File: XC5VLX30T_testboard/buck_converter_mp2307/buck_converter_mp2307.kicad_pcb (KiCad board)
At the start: 2 copper layers, 18.5 x 11.8 mm, 12 parts, among them J1 Conn_02x01, J4 Conn_01x06_Pin, U1 MP2307DN-LF-Z

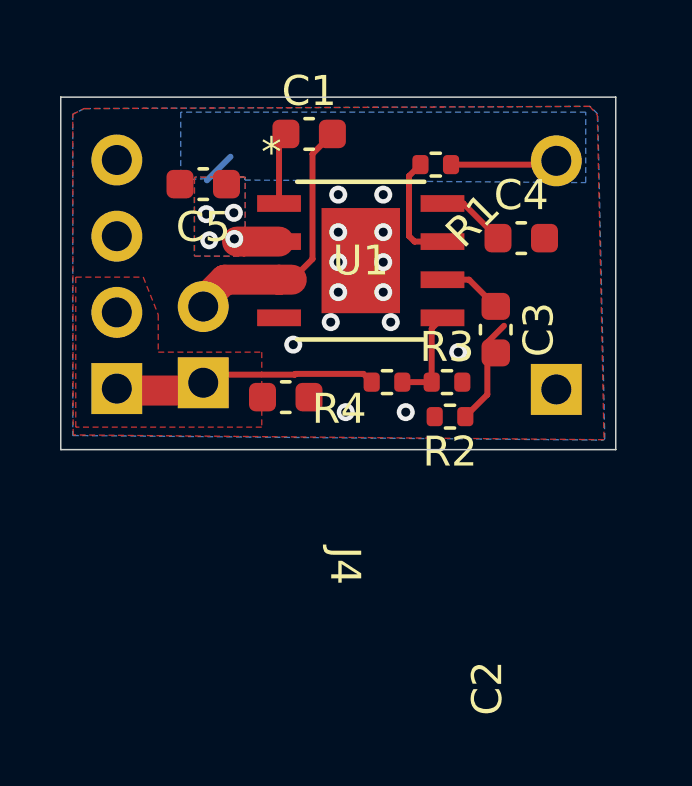
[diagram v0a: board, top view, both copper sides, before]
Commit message: reordered headers
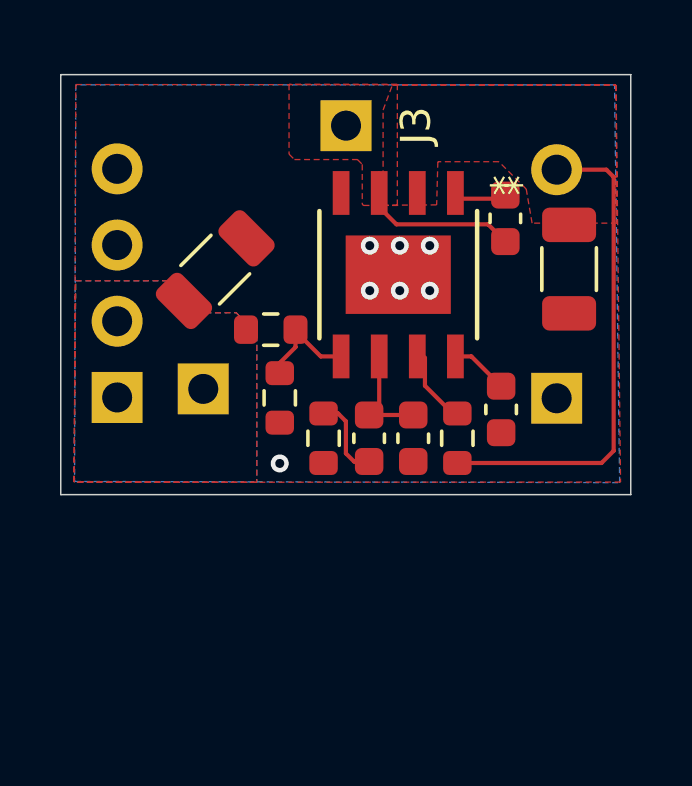
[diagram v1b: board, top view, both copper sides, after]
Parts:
- removed C5: 22uF, Capacitor_SMD:C_0603_1608Metric
- removed J1: Conn_02x01, Connector_PinHeader_2.54mm:PinHeader_2x01_P2.54mm_Vertical
- added C6: 0.1uF, Capacitor_SMD:C_0603_1608Metric, F.Cu at (117.5, 91.4)
- added C8: 22uF, Capacitor_SMD:C_1206_3216Metric, F.Cu at (122.7, 85.7)
- added J2: Inductor L, Connector_PinHeader_2.54mm:PinHeader_1x01_P2.54mm_Vertical, F.Cu at (110.5, 89.7)
- added J3: Inductor_R, Connector_PinHeader_2.54mm:PinHeader_1x01_P2.54mm_Vertical, F.Cu at (115.3, 81.0)
- C2: footprint Capacitor_SMD:C_0603_1608Metric -> Capacitor_SMD:C_1206_3216Metric
- R1, R2, R3, R4: footprint Resistor_SMD:R_0402_1005Metric -> Resistor_SMD:R_0603_1608Metric
- moved R1 9.15 mm to (119.0, 91.4), turned to 90 degrees
- moved C1 7.12 mm to (120.6, 84.0), turned to -90 degrees
- moved C4 5.75 mm to (120.4, 90.4), turned to -90 degrees
- moved R3 5.60 mm to (113.0, 90.0), turned to -90 degrees
- moved C3 5.56 mm to (116.0, 91.4)
- moved C2 4.86 mm to (110.9, 85.8), turned to 45 degrees
- moved R2 4.28 mm to (114.5, 91.4), turned to -90 degrees
- moved R4 4.25 mm to (112.8, 87.8)
- moved U1 1.33 mm to (117.0, 85.9), turned to -90 degrees
- moved J4 0.30 mm to (114.7, 95.9)
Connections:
- net Net-(J1-Pin_2) renamed SWITCHED
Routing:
- net vccext: track 6.20 -> 17.7 mm, vias 4 -> 0
- net VCCoutput: track 8.03 -> 0.00 mm
- net SWITCHED: track 9.08 -> 5.82 mm
- net Net-(U1-EN): track 3.73 -> 2.40 mm
- net Net-(C3-Pad2): track 3.56 -> 2.81 mm
- net Net-(U1-COMP): track 2.14 -> 2.83 mm
- net Net-(U1-BS): track 2.35 -> 1.75 mm
- net GND: vias 14 -> 7
- added copper zone on F.Cu, net SWITCHED
- added copper zone on B.Cu, net VCCoutput
- removed copper zone on B.Cu, net vccext
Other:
- board size 18.5 x 11.8 mm -> 19 x 14 mm

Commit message: added tht version of mp2307 board
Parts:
- added R5: R, Resistor_THT:R_Axial_DIN0204_L3.6mm_D1.6mm_P1.90mm_Vertical, F.Cu at (1.07, 1.07)
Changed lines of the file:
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@@
 	(net 9 "VCCoutput")
 	(net 10 "SWITCHED")
+	(net 11 "unconnected-(R5-Pad2)")
+	(net 12 "unconnected-(R5-Pad1)")
 	(footprint "Capacitor_SMD:C_0603_1608Metric"
 		(layer "F.Cu")
@@
 			(unlocked yes)
 			(layer "F.SilkS")
-			(hide yes)
 			(effects
 				(font
@@
 			(unlocked yes)
 			(layer "F.Fab")
-			(hide yes)
 			(effects
 				(font
@@
 		)
 		(property "Footprint" "IC8_MP2307_MNP"
-			(at 0 0 90)
+			(at 0 0 -90)
 			(layer "F.Fab")
 			(hide yes)
@@
 		)
 		(property "Datasheet" "MP2307DN-LF-Z"
-			(at 0 0 90)
+			(at 0 0 -90)
 			(layer "F.Fab")
 			(hide yes)
@@
 		)
 		(property "Description" ""
-			(at 0 0 90)
+			(at 0 0 -90)
 			(layer "F.Fab")
 			(hide yes)
@@
 		)
 		(fp_text user "*"
-			(at -2.97815 -3.6068 90)
+			(at -2.97815 -3.6068 -90)
+			(unlocked yes)
 			(layer "F.SilkS")
 			(effects
@@
 		(fp_text user "*"
 			(at -2.97815 -3.6068 -90)
-			(unlocked yes)
-			(layer "F.SilkS")
-			(effects
-				(font
-					(size 1 1)
-					(thickness 0.15)
-				)
-			)
-		)
-		(fp_text user "*"
-			(at -1.6129 -2.4257 90)
-			(layer "F.Fab")
+			(layer "F.SilkS")
 			(effects
 				(font
@@
 			(at 0 0 -90)
 			(unlocked yes)
+			(layer "F.Fab")
+			(effects
+				(font
+					(size 1 1)
+					(thickness 0.15)
+				)
+			)
+		)
+		(fp_text user "*"
+			(at -1.6129 -2.4257 -90)
 			(layer "F.Fab")
 			(effects
@@
 			(pinfunction "IN")
 			(pintype "unspecified")
-			(zone_connect 2)
 		)
 		(pad "3" smd rect
@@
 			(pinfunction "SW")
 			(pintype "unspecified")
-			(zone_connect 2)
 		)
 		(pad "4" smd rect
@@
 		(tags "resistor")
 		(property "Reference" "R4"
-			(at 0 -1.43 360)
+			(at 0 -1.43 0)
 			(layer "F.SilkS")
 			(hide yes)
@@
 		)
 		(property "Value" "220"
-			(at 0 1.43 360)
+			(at 0 1.43 0)
 			(layer "F.Fab")
 			(hide yes)
@@
 		)
 		(fp_text user "${REFERENCE}"
-			(at 0 0 360)
+			(at 0 0 0)
 			(layer "F.Fab")
 			(effects
@@
 			(offset
 				(xyz 0 0 0)
+			)
+			(scale
+				(xyz 1 1 1)
+			)
+			(rotate
+				(xyz 0 0 0)
+			)
+		)
+	)
+	(footprint "Resistor_THT:R_Axial_DIN0204_L3.6mm_D1.6mm_P1.90mm_Vertical"
+		(layer "F.Cu")
+		(at 1.075 1.075)
+		(descr "Resistor, Axial_DIN0204 series, Axial, Vertical, pin pitch=1.9mm, 0.167W, length*diameter=3.6*1.6mm^2, http://cdn-reichelt.de/documents/datenblatt/B400/1_4W%23YAG.pdf")
+		(tags "Resistor Axial_DIN0204 series Axial Vertical pin pitch 1.9mm 0.167W length 3.6mm diameter 1.6mm")
+		(property "Reference" "R5"
+			(at 0.95 -1.92 0)
+			(layer "F.SilkS")
+			(effects
+				(font
+					(size 1 1)
+					(thickness 0.15)
+				)
+			)
+		)
+		(property "Value" "R"
+			(at 0.95 1.92 0)
+			(layer "F.Fab")
+			(effects
+				(font
+					(size 1 1)
+					(thickness 0.15)
+				)
+			)
+		)
+		(property "Footprint" "Resistor_THT:R_Axial_DIN0204_L3.6mm_D1.6mm_P1.90mm_Vertical"
+			(at 0 0 0)
+			(unlocked yes)
+			(layer "F.Fab")
+			(hide yes)
+			(effects
+				(font
+					(size 1.27 1.27)
+					(thickness 0.15)
+				)
+			)
+		)
+		(property "Datasheet" ""
+			(at 0 0 0)
+			(unlocked yes)
+			(layer "F.Fab")
+			(hide yes)
+			(effects
+				(font
+					(size 1.27 1.27)
+					(thickness 0.15)
+				)
+			)
+		)
+		(property "Description" "Resistor"
+			(at 0 0 0)
+			(unlocked yes)
+			(layer "F.Fab")
+			(hide yes)
+			(effects
+				(font
+					(size 1.27 1.27)
+					(thickness 0.15)
+				)
+			)
+		)
+		(property ki_fp_filters "R_*")
+		(sheetname "Root")
+		(sheetfile "buck_converter_mp2307.kicad_sch")
+		(attr through_hole)
+		(fp_arc
+			(start 0.320095 0.749359)
+			(mid -0.813042 -0.054435)
+			(end 0.417133 -0.7)
+			(stroke
+				(width 0.12)
+				(type solid)
+			)
+			(layer "F.SilkS")
+		)
+		(fp_line
+			(start -1.05 -1.05)
+			(end -1.05 1.05)
+			(stroke
+				(width 0.05)
+				(type solid)
+			)
+			(layer "F.CrtYd")
+		)
+		(fp_line
+			(start -1.05 1.05)
+			(end 2.86 1.05)
+			(stroke
+				(width 0.05)
+				(type solid)
+			)
+			(layer "F.CrtYd")
+		)
+		(fp_line
+			(start 2.86 -1.05)
+			(end -1.05 -1.05)
+			(stroke
+				(width 0.05)
+				(type solid)
+			)
+			(layer "F.CrtYd")
+		)
+		(fp_line
+			(start 2.86 1.05)
+			(end 2.86 -1.05)
+			(stroke
+				(width 0.05)
+				(type solid)
+			)
+			(layer "F.CrtYd")
+		)
+		(fp_line
+			(start 0 0)
+			(end 1.9 0)
+			(stroke
+				(width 0.1)
+				(type solid)
+			)
+			(layer "F.Fab")
+		)
+		(fp_circle
+			(center 0 0)
+			(end 0.8 0)
+			(stroke
+				(width 0.1)
+				(type solid)
+			)
+			(fill none)
+			(layer "F.Fab")
+		)
+		(fp_text user "${REFERENCE}"
+			(at 0.95 -1.92 0)
+			(layer "F.Fab")
+			(effects
+				(font
+					(size 1 1)
+					(thickness 0.15)
+				)
+			)
+		)
+		(pad "1" thru_hole circle
+			(at 0 0)
+			(size 1.4 1.4)
+			(drill 0.7)
+			(layers "*.Cu" "*.Mask")
+			(remove_unused_layers no)
+			(net 12 "unconnected-(R5-Pad1)")
+			(pintype "passive")
+		)
+		(pad "2" thru_hole oval
+			(at 1.9 0)
+			(size 1.4 1.4)
+			(drill 0.7)
+			(layers "*.Cu" "*.Mask")
+			(remove_unused_layers no)
+			(net 11 "unconnected-(R5-Pad2)")
+			(pintype "passive")
+		)
+		(model "${KICAD8_3DMODEL_DIR}/Resistor_THT.3dshapes/R_Axial_DIN0204_L3.6mm_D1.6mm_P1.90mm_Vertical.wrl"
+			(offset
+				(xyz 0 0 0)
